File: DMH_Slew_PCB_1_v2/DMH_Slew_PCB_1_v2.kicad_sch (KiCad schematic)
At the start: 0 parts

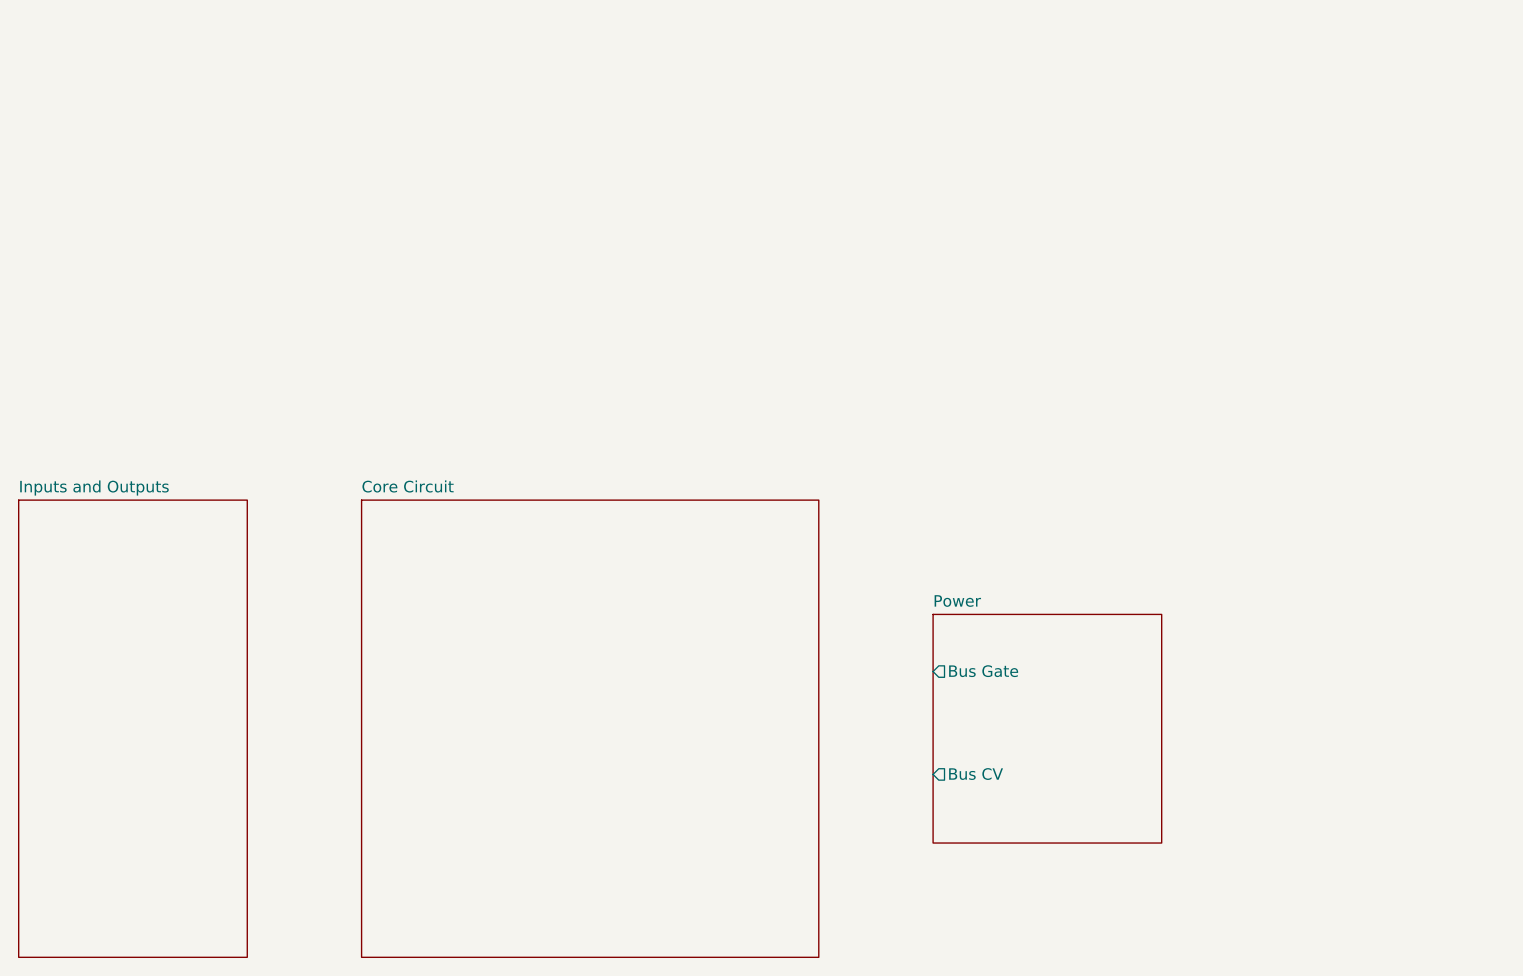
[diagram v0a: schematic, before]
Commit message: Added state gate outputs circuit
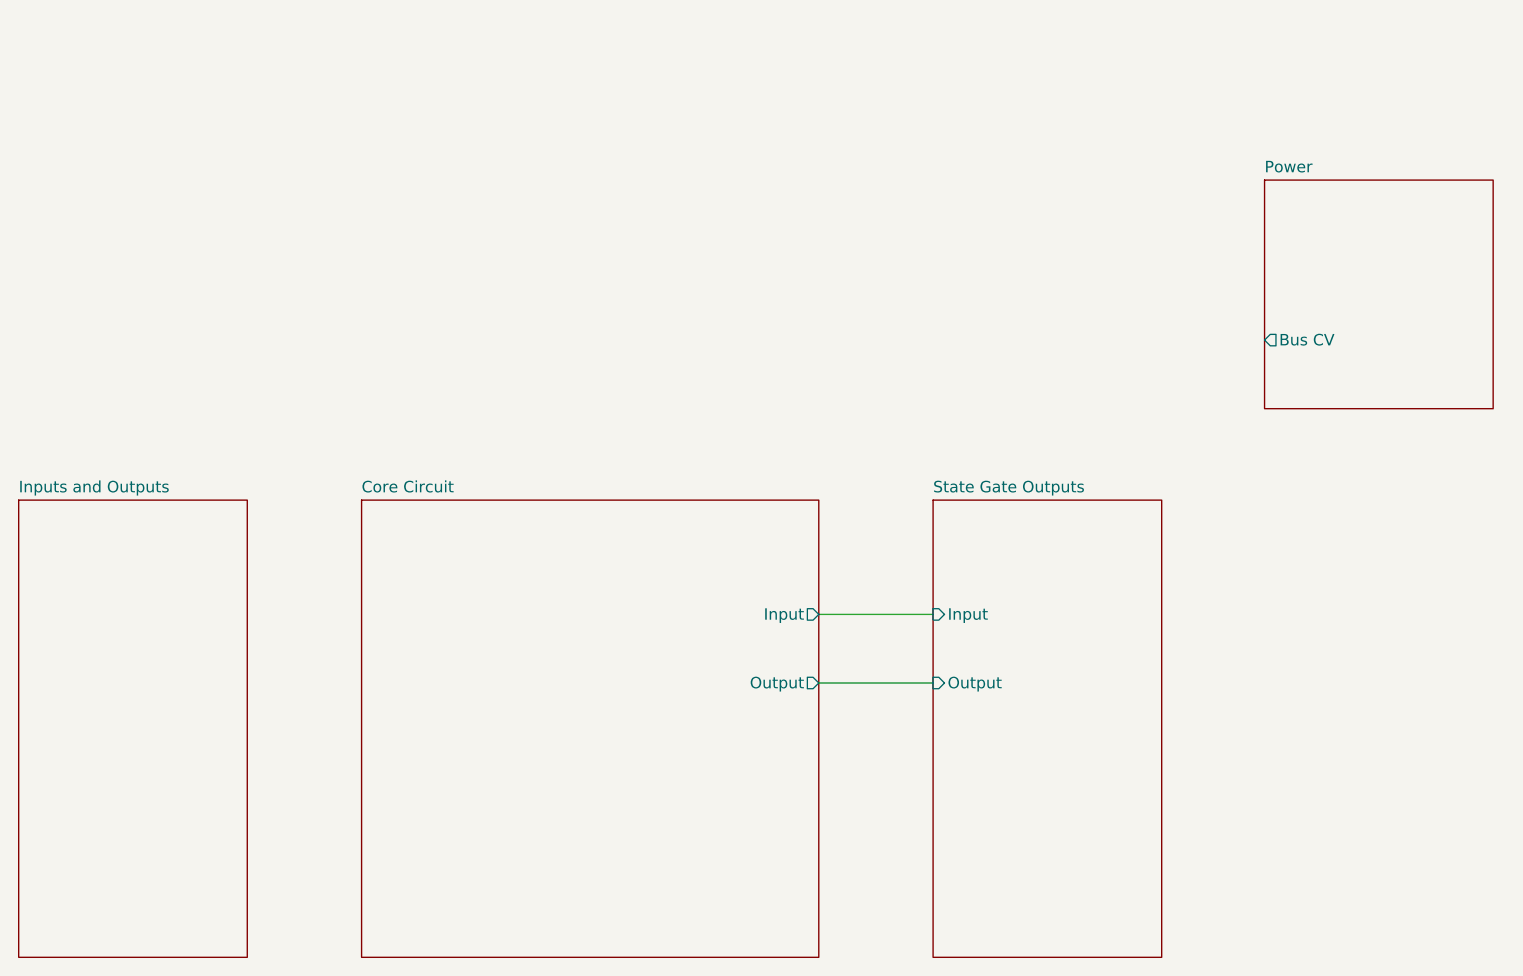
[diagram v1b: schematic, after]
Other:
- added sheet State Gate Outputs (State_gate_outputs.kicad_sch)
- sheet Core Circuit ports: added Input, Output; removed none
- sheet Power ports: added none; removed Bus Gate
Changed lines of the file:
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@@
 		(comment 1 "PCB for 5 cm Kosmo format synthesizer module")
 	)
+	(wire
+		(pts
+			(xy 114.3 96.52) (xy 127 96.52)
+		)
+		(stroke
+			(width 0)
+			(type default)
+		)
+	)
+	(wire
+		(pts
+			(xy 114.3 88.9) (xy 127 88.9)
+		)
+		(stroke
+			(width 0)
+			(type default)
+		)
+	)
 	(sheet
-		(at 127 88.9)
+		(at 163.83 40.64)
 		(size 25.4 25.4)
 		(exclude_from_sim no)
@@
 		)
 		(property "Sheetname" "Power"
-			(at 127 88.1884 0)
+			(at 163.83 39.9284 0)
 			(effects
 				(font
@@
 		)
 		(property "Sheetfile" "Power.kicad_sch"
-			(at 127 114.8846 0)
+			(at 163.83 66.6246 0)
 			(effects
 				(font
@@
 			)
 		)
-		(pin "Bus Gate" output
-			(at 127 95.25 180)
-			(effects
-				(font
-					(size 1.27 1.27)
-				)
-				(justify left)
-			)
-		)
 		(pin "Bus CV" output
-			(at 127 106.68 180)
+			(at 163.83 58.42 180)
 			(effects
 				(font
@@
 				(path "/58f4306d-5387-4983-bb08-41a2313fd315"
 					(page "4")
+				)
+			)
+		)
+	)
+	(sheet
+		(at 127 76.2)
+		(size 25.4 50.8)
+		(exclude_from_sim no)
+		(in_bom yes)
+		(on_board yes)
+		(dnp no)
+		(fields_autoplaced yes)
+		(stroke
+			(width 0.1524)
+			(type solid)
+		)
+		(fill
+			(color 0 0 0 0.0000)
+		)
+		(property "Sheetname" "State Gate Outputs"
+			(at 127 75.4884 0)
+			(effects
+				(font
+					(size 1.27 1.27)
+				)
+				(justify left bottom)
+			)
+		)
+		(property "Sheetfile" "State_gate_outputs.kicad_sch"
+			(at 127 127.5846 0)
+			(effects
+				(font
+					(size 1.27 1.27)
+				)
+				(justify left top)
+				(hide yes)
+			)
+		)
+		(pin "Input" input
+			(at 127 88.9 180)
+			(effects
+				(font
+					(size 1.27 1.27)
+				)
+				(justify left)
+			)
+		)
+		(pin "Output" input
+			(at 127 96.52 180)
+			(effects
+				(font
+					(size 1.27 1.27)
+				)
+				(justify left)
+			)
+		)
+		(instances
+			(project "DMH_Slew_PCB_1_v2"
+				(path "/58f4306d-5387-4983-bb08-41a2313fd315"
+					(page "5")
 				)
 			)
@@
 			)
 		)
+		(pin "Input" output
+			(at 114.3 88.9 0)
+			(effects
+				(font
+					(size 1.27 1.27)
+				)
+				(justify right)
+			)
+		)
+		(pin "Output" output
+			(at 114.3 96.52 0)
+			(effects
+				(font
+					(size 1.27 1.27)
+				)
+				(justify right)
+			)
+		)

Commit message: Preparing for pcb design
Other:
- sheet Inputs and Outputs renamed Mother Board
- added sheet Controls Board (Controls_board.kicad_sch)
- sheet Mother Board: file Inputs_and_Outputs.kicad_sch -> Mother_board.kicad_sch
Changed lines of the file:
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@@
 	(wire
 		(pts
-			(xy 114.3 96.52) (xy 127 96.52)
+			(xy 114.3 45.72) (xy 127 45.72)
 		)
 		(stroke
@@
 	(wire
 		(pts
-			(xy 114.3 88.9) (xy 127 88.9)
+			(xy 114.3 38.1) (xy 127 38.1)
 		)
 		(stroke
@@
 	)
 	(sheet
-		(at 163.83 40.64)
+		(at 165.1 38.1)
 		(size 25.4 25.4)
 		(exclude_from_sim no)
@@
 		)
 		(property "Sheetname" "Power"
-			(at 163.83 39.9284 0)
+			(at 165.1 37.3884 0)
 			(effects
 				(font
@@
 		)
 		(property "Sheetfile" "Power.kicad_sch"
-			(at 163.83 66.6246 0)
+			(at 165.1 64.0846 0)
 			(effects
 				(font
@@
 		)
 		(pin "Bus CV" output
-			(at 163.83 58.42 180)
+			(at 165.1 55.88 180)
 			(effects
 				(font
@@
 	)
 	(sheet
-		(at 127 76.2)
+		(at 25.4 88.9)
+		(size 25.4 38.1)
+		(exclude_from_sim no)
+		(in_bom yes)
+		(on_board yes)
+		(dnp no)
+		(fields_autoplaced yes)
+		(stroke
+			(width 0.1524)
+			(type solid)
+		)
+		(fill
+			(color 0 0 0 0.0000)
+		)
+		(property "Sheetname" "Controls Board"
+			(at 25.4 88.1884 0)
+			(effects
+				(font
+					(size 1.27 1.27)
+				)
+				(justify left bottom)
+			)
+		)
+		(property "Sheetfile" "Controls_board.kicad_sch"
+			(at 25.4 127.5846 0)
+			(effects
+				(font
+					(size 1.27 1.27)
+				)
+				(justify left top)
+				(hide yes)
+			)
+		)
+		(instances
+			(project "DMH_Slew_PCB_1_v2"
+				(path "/58f4306d-5387-4983-bb08-41a2313fd315"
+					(page "6")
+				)
+			)
+		)
+	)
+	(sheet
+		(at 127 25.4)
 		(size 25.4 50.8)
 		(exclude_from_sim no)
@@
 		)
 		(property "Sheetname" "State Gate Outputs"
-			(at 127 75.4884 0)
+			(at 127 24.6884 0)
 			(effects
 				(font
@@
 		)
 		(property "Sheetfile" "State_gate_outputs.kicad_sch"
-			(at 127 127.5846 0)
+			(at 127 76.7846 0)
 			(effects
 				(font
@@
 		)
 		(pin "Input" input
-			(at 127 88.9 180)
+			(at 127 38.1 180)
 			(effects
 				(font
@@
 		)
 		(pin "Output" input
-			(at 127 96.52 180)
+			(at 127 45.72 180)
 			(effects
 				(font
@@
 	)
 	(sheet
-		(at 63.5 76.2)
+		(at 63.5 25.4)
 		(size 50.8 50.8)
 		(exclude_from_sim no)
@@
 		)
 		(property "Sheetname" "Core Circuit"
-			(at 63.5 75.4884 0)
+			(at 63.5 24.6884 0)
 			(effects
 				(font
@@
 		)
 		(property "Sheetfile" "Core_Circuit.kicad_sch"
-			(at 63.5 127.5846 0)
+			(at 63.5 76.7846 0)
 			(effects
 				(font
@@
 		)
 		(pin "Input" output
-			(at 114.3 88.9 0)
+			(at 114.3 38.1 0)
 			(effects
 				(font
@@
 		)
 		(pin "Output" output
-			(at 114.3 96.52 0)
+			(at 114.3 45.72 0)
 			(effects
 				(font
@@
 	)
 	(sheet
-		(at 25.4 76.2)
+		(at 25.4 25.4)
 		(size 25.4 50.8)
 		(exclude_from_sim no)
@@
 			(color 0 0 0 0.0000)
 		)
-		(property "Sheetname" "Inputs and Outputs"
-			(at 25.4 75.4884 0)
-			(effects
-				(font
-					(size 1.27 1.27)
-				)
-				(justify left bottom)
-			)
-		)
-		(property "Sheetfile" "Inputs_and_Outputs.kicad_sch"
-			(at 25.4 127.5846 0)
-			(effects
-				(font
+		(property "Sheetname" "Mother Board"
+			(at 25.4 24.6884 0)
+			(effects
+				(font
+					(size 1.27 1.27)
+				)
+				(justify left bottom)
+			)
+		)
+		(property "Sheetfile" "Mother_board.kicad_sch"
+			(at 25.4 76.7846 0)
+			(effects
+				(font

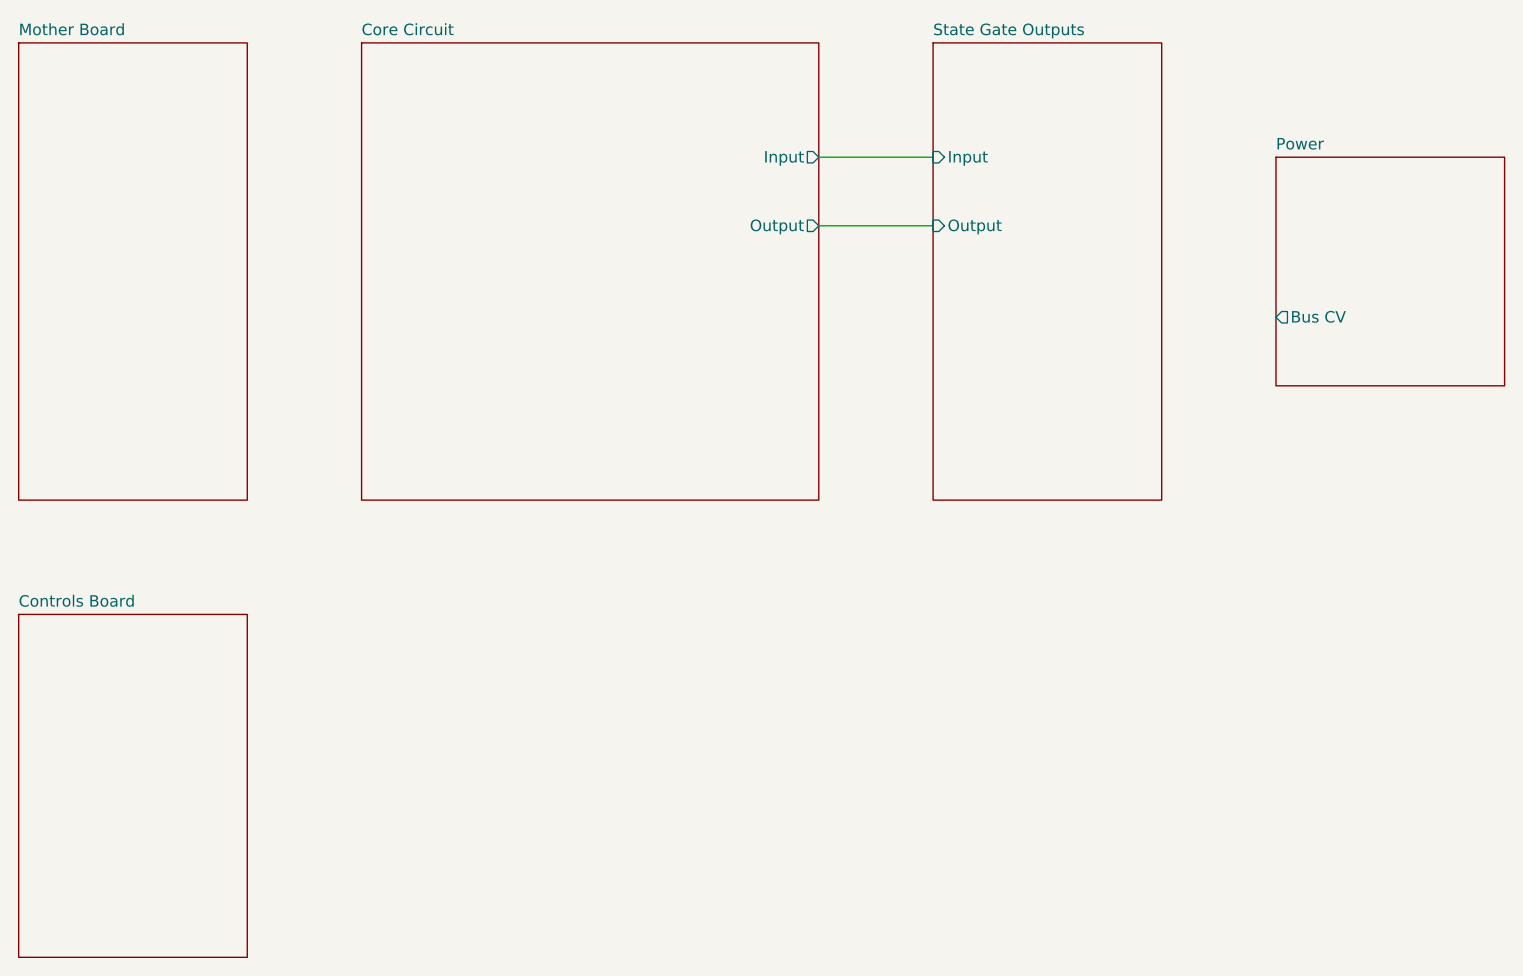
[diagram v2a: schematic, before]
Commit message: Separating PCB 1 and 2 in schematic
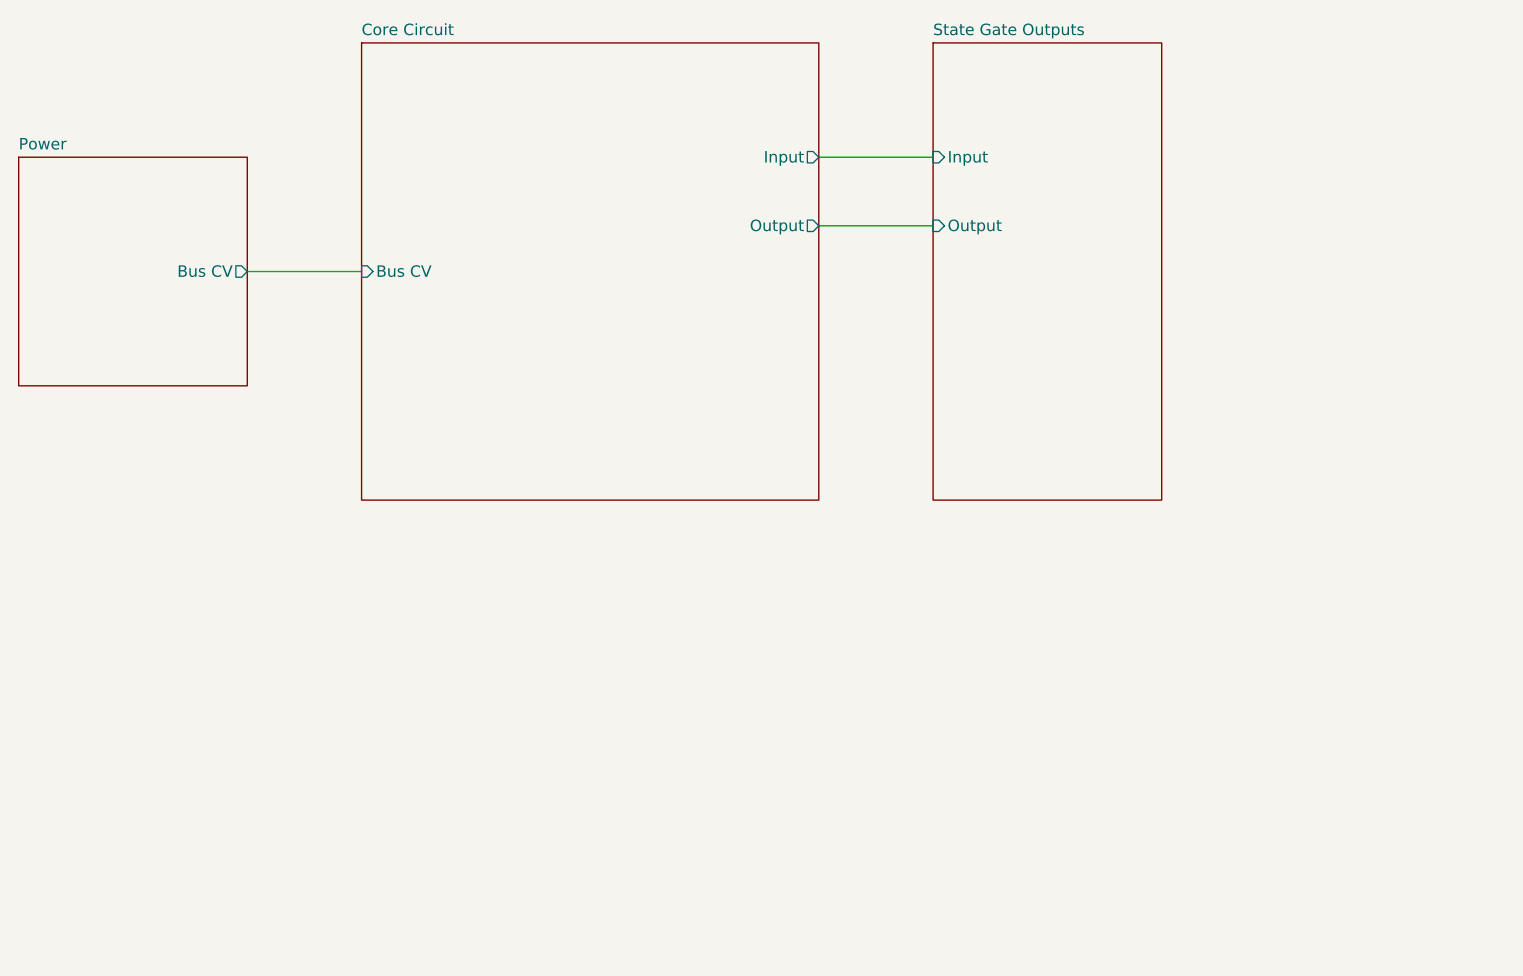
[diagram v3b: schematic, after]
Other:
- removed sheet Controls Board
- removed sheet Mother Board
- sheet Core Circuit ports: added Bus CV; removed none
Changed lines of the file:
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@@
+		)
+	)
+	(wire
+		(pts
+			(xy 50.8 50.8) (xy 63.5 50.8)
+		)
+		(stroke
+			(width 0)
+			(type default)
 		)
 	)
 	(sheet
-		(at 165.1 38.1)
+		(at 25.4 38.1)
 		(size 25.4 25.4)
 		(exclude_from_sim no)
@@
 		)
 		(property "Sheetname" "Power"
-			(at 165.1 37.3884 0)
+			(at 25.4 37.3884 0)
 			(effects
 				(font
@@
 		)
 		(property "Sheetfile" "Power.kicad_sch"
-			(at 165.1 64.0846 0)
+			(at 25.4 64.0846 0)
 			(effects
 				(font
@@
 		)
 		(pin "Bus CV" output
-			(at 165.1 55.88 180)
+			(at 50.8 50.8 0)
 			(effects
 				(font
 					(size 1.27 1.27)
 				)
-				(justify left)
+				(justify right)
 			)
 		)
@@
 				(path "/58f4306d-5387-4983-bb08-41a2313fd315"
 					(page "4")
-				)
-			)
-		)
-	)
-	(sheet
-		(at 25.4 88.9)
-		(size 25.4 38.1)
-		(exclude_from_sim no)
-		(in_bom yes)
-		(on_board yes)
-		(dnp no)
-		(fields_autoplaced yes)
-		(stroke
-			(width 0.1524)
-			(type solid)
-		)
-		(fill
-			(color 0 0 0 0.0000)
-		)
-		(property "Sheetname" "Controls Board"
-			(at 25.4 88.1884 0)
-			(effects
-				(font
-					(size 1.27 1.27)
-				)
-				(justify left bottom)
-			)
-		)
-		(property "Sheetfile" "Controls_board.kicad_sch"
-			(at 25.4 127.5846 0)
-			(effects
-				(font
-					(size 1.27 1.27)
-				)
-				(justify left top)
-				(hide yes)
-			)
-		)
-		(instances
-			(project "DMH_Slew_PCB_1_v2"
-				(path "/58f4306d-5387-4983-bb08-41a2313fd315"
-					(page "6")
 				)
 			)
@@
 			)
 		)
+		(pin "Bus CV" input
+			(at 63.5 50.8 180)
+			(effects
+				(font
+					(size 1.27 1.27)
+				)
+				(justify left)
+			)
+		)
 		(instances
 			(project "DMH_Slew_PCB_1_v2"
@@
 				)
 			)
-		)
-	)
-	(sheet
-		(at 25.4 25.4)
-		(size 25.4 50.8)
-		(exclude_from_sim no)
-		(in_bom yes)
-		(on_board yes)
-		(dnp no)
-		(fields_autoplaced yes)
-		(stroke
-			(width 0.1524)
-			(type solid)
-		)
-		(fill
-			(color 0 0 0 0.0000)
-		)
-		(property "Sheetname" "Mother Board"
-			(at 25.4 24.6884 0)
-			(effects
-				(font
-					(size 1.27 1.27)
-				)
-				(justify left bottom)
-			)
-		)
-		(property "Sheetfile" "Mother_board.kicad_sch"
-			(at 25.4 76.7846 0)
-			(effects
-				(font
-					(size 1.27 1.27)
-				)
-				(justify left top)
-				(hide yes)
-			)
-		)
-		(instances
-			(project "DMH_Slew_PCB_1_v2"
-				(path "/58f4306d-5387-4983-bb08-41a2313fd315"
-					(page "2")
-				)
-			)
